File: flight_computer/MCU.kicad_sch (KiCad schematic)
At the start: 43 parts, among them J1 Conn_02x05_Odd_Even, J2 MEM2061-01-188-00-A_REVA, Q1 Q_NPN_BEC, SW1 SW_Push, SW2 SW_Push, U2 STM8S007C8T6TR, Y1 12MHz

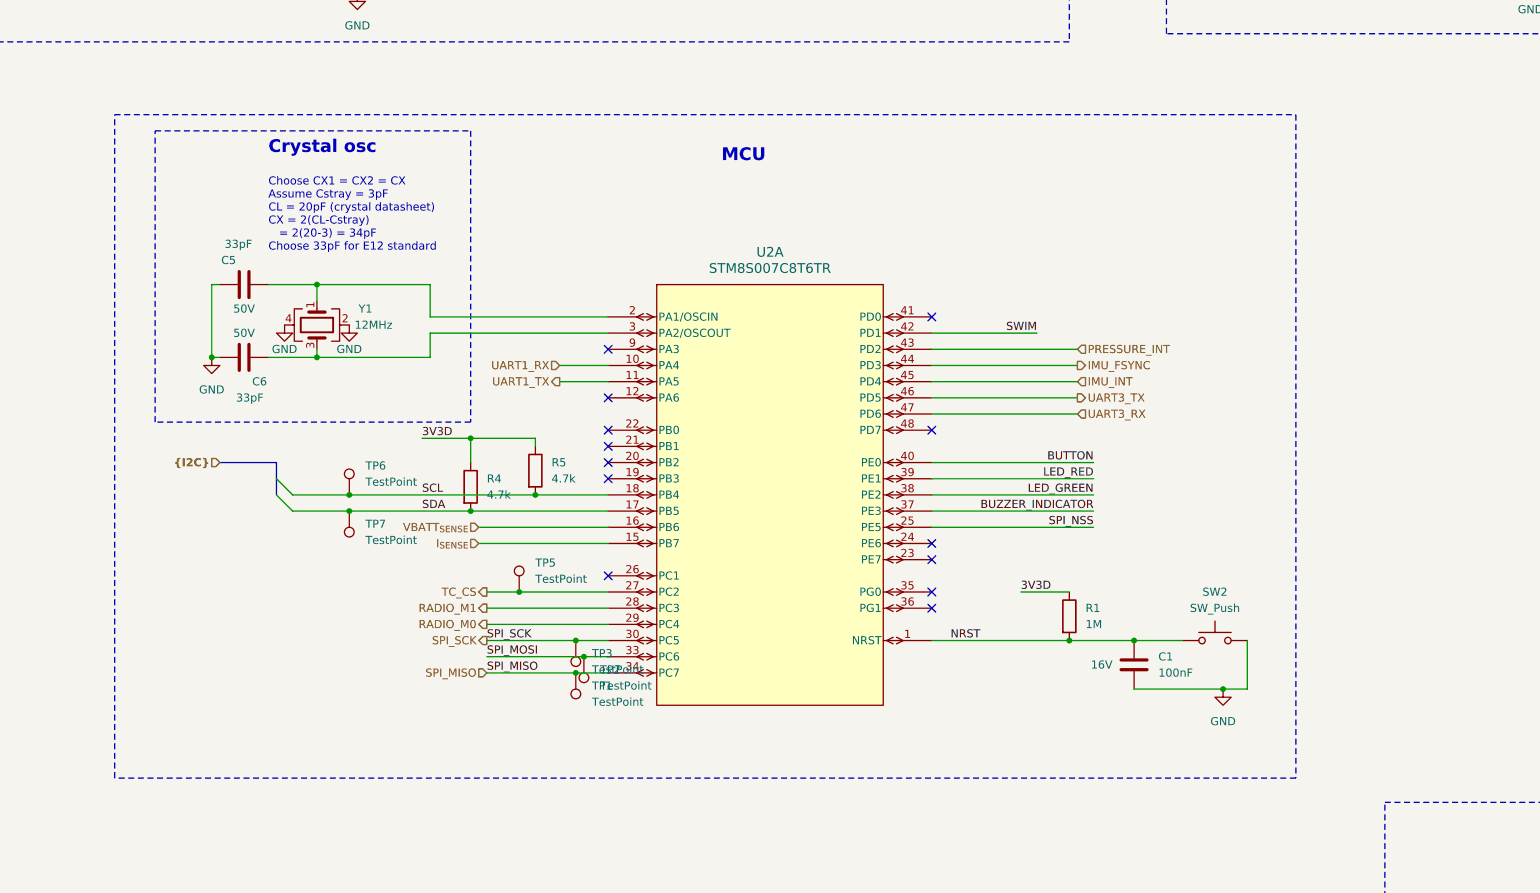
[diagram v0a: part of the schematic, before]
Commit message: First draft of PCB routing complete
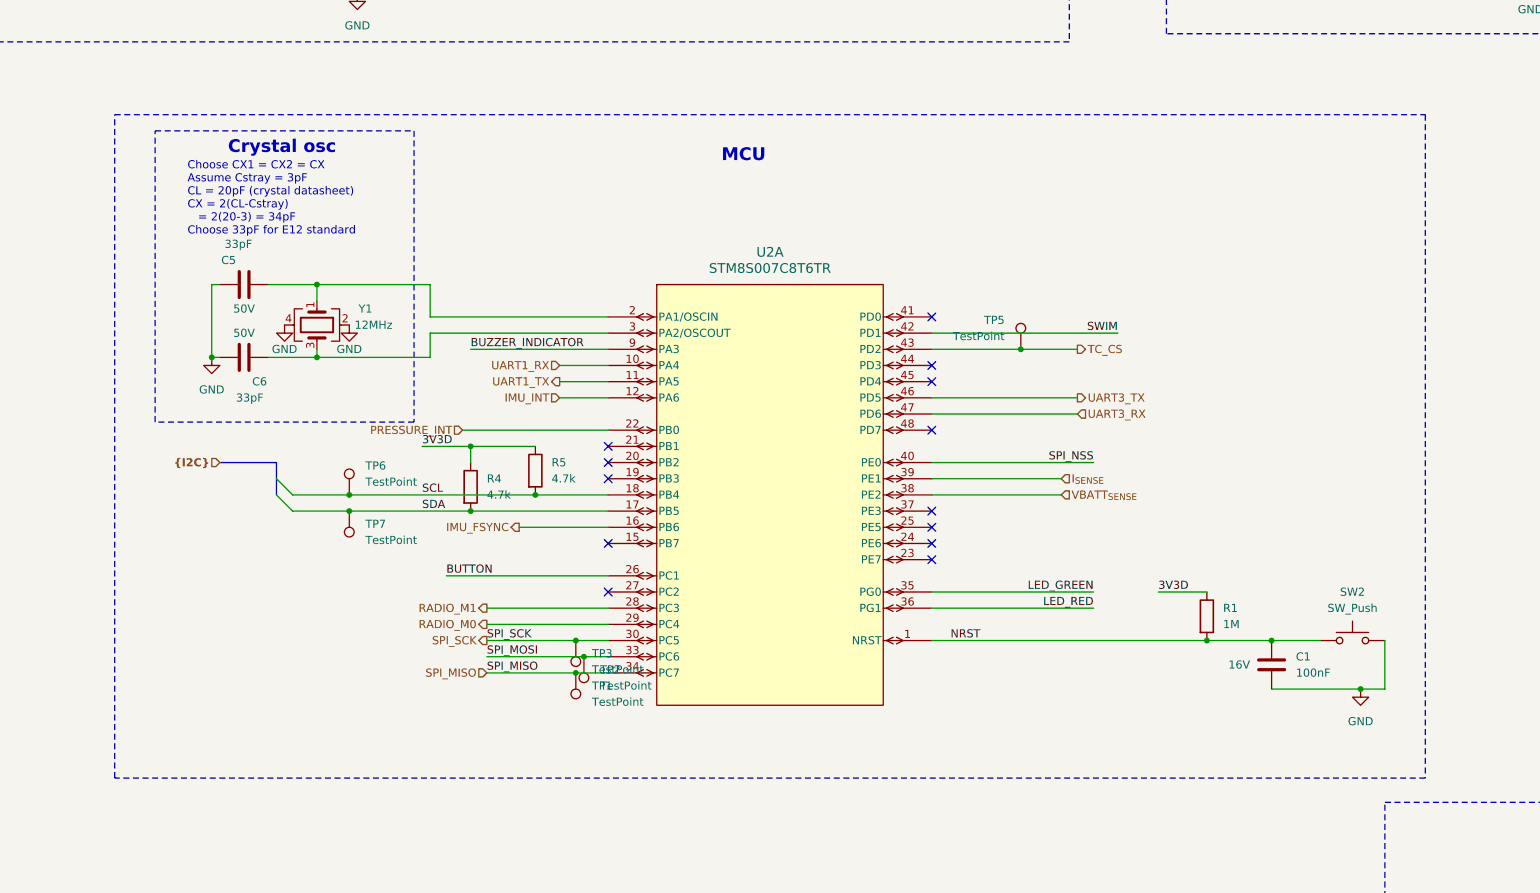
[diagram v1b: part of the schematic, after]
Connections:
- net BUTTON: now also U2.26 (PC1); no longer U2.40 (PE0)
- net BUZZER_INDICATOR: now also U2.9 (PA3); no longer U2.37 (PE3)
- net IMU_FSYNC: now also U2.16 (PB6); no longer U2.44 (PD3)
- net IMU_INT: now also U2.12 (PA6); no longer U2.45 (PD4)
- net I_{SENSE}: now also U2.39 (PE1); no longer U2.15 (PB7)
- net LED_GREEN: now also U2.35 (PG0); no longer U2.38 (PE2)
- net LED_RED: now also U2.36 (PG1); no longer U2.39 (PE1)
- net PRESSURE_INT: now also U2.22 (PB0); no longer U2.43 (PD2)
- net SPI_NSS: now also U2.40 (PE0); no longer U2.25 (PE5)
- net TC_CS: now also U2.43 (PD2); no longer U2.27 (PC2)
- net VBATT_{SENSE}: now also U2.38 (PE2); no longer U2.16 (PB6)
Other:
- moved on the sheet: C1, R1, SW2, TP5

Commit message: start of esp32
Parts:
- added C1 (x5): 100nF, Capacitor_SMD:C_0402_1005Metric, symbol Device:C
- added C1 (x2): DNP, Capacitor_SMD:C_0402_1005Metric, symbol Device:C
- added C12: 10uF, Capacitor_SMD:C_0402_1005Metric, symbol Device:C
- added C18: 10nF, Capacitor_SMD:C_0402_1005Metric, symbol Device:C
- added C40, C53: ~, Capacitor_SMD:C_0402_1005Metric, symbol Device:C
- added C46, C48, C50: 1uF, Capacitor_SMD:C_0402_1005Metric, symbol Device:C
- added L3: 0.1nH, symbol Device:L
- added L4: 24nH, symbol Device:L
- added R1: 1M, Resistor_SMD:R_0402_1005Metric, symbol Device:R
- added R31, R32, R35, R36, R37, R38, R39, R40, R41: 0R, Resistor_SMD:R_0402_1005Metric, symbol Device:R
- added R34: DNP, Resistor_SMD:R_0402_1005Metric, symbol Device:R
- added U10: ESP32-S3, Package_DFN_QFN:QFN-56-1EP_7x7mm_P0.4mm_EP5.6x5.6mm, symbol Espressif:ESP32-S3
- added Y2: 40MHz, Crystal:Crystal_SMD_3225-4Pin_3.2x2.5mm, symbol Device:Crystal_GND24
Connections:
- net 3V3A: now also C18.1, C50.1, U10.55 (VDDA), U10.56 (VDDA)
- net 3V3D: now also C1.1, C1.1, C1.1, C1.1, C12.1, C46.1, C48.1, L3.1, R1.1, R34.2, U10.20 (VDD3P3_RTC), U10.29 (VDD_SPI), U10.46 (VDD3P3_CPU)
- net GND: now also C1.1, C1.2, C1.2, C1.2, C1.2, C1.2, C1.2, C12.2, C18.2, C40.1, C46.2, C48.2, C50.2, C53.1, U10.57 (GND), Y2.2, Y2.4
- net NRST: no longer C1.1, R1.2, SW2.1, U2.1 (NRST)
- new net: C1.1, R1.2, SW2.1, U10.4 (CHIP_PU/RESET)
- new net: R37.1, U10.30 (SPIHD/GPIO27)
- new net: C53.2, L4.1, Y2.3
- new net: L4.2, U10.54 (XTAL_P)
- new net: C1.2, R1.2, R31.2
- new net: R31.1, U10.26 (GPIO20/USB_D+/ADC2_CH9)
- new net: R32.1, U10.25 (GPIO19/USB_D-/ADC2_CH8)
- new net: C1.1, R32.2
- new net: R38.1, U10.31 (SPIWP/GPIO28)
- new net: R34.1, U10.51 (GPIO45)
- new net: C40.2, U10.53 (XTAL_N), Y2.1
- new net: R39.1, U10.33 (SPICLK/GPIO30)
- new net: R40.1, U10.34 (SPIQ/GPIO31)
- new net: R41.1, U10.35 (SPID/GPIO32)
- new net: R35.2, U10.49 (U0TXD/PROG/GPIO43)
- new net: R36.2, U10.50 (U0RXD/PROG/GPIO44)
- new net VDD3P3: C1.1, L3.2, U10.2 (VDD3P3), U10.3 (VDD3P3)
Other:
- note added: "https://docs.espressif.com/projects/esp-hardware-design-guidelines/en/latest/esp32s3/esp-hardware-design-guidelines-en-master-esp32s3.pdf"
- note added: "https://www.espressif.com/sites/default/files/documentation/esp32-s3_datasheet_en.pdf"
- note added: "https://www.espressif.com/sites/default/files/documentation/esp32-s3_technical_reference_manual_en.pdf"
- moved on the sheet: C1, R1, SW2

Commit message: RevB PCB work
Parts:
- removed C1: 100nF, Capacitor_SMD:C_0402_1005Metric, symbol Device:C
- removed C48: 1uF, Capacitor_SMD:C_0402_1005Metric, symbol Device:C
- removed R37, R38, R39, R40, R41: 0R, Resistor_SMD:R_0402_1005Metric, symbol Device:R
- added J6: USB_C_Receptacle_USB2.0, symbol Connector:USB_C_Receptacle_USB2.0
- added R42: 5.1k, Resistor_SMD:R_0402_1005Metric, symbol Device:R
- added U11: USBLC6-2SC6, Package_TO_SOT_SMD:SOT-23-6, symbol Power_Protection:USBLC6-2SC6
- added U12: ESP32-S3-WROOM-1, PCM_Espressif:ESP32-S3-WROOM-1, symbol Espressif:ESP32-S3-WROOM-1
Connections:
- net 3V3D: no longer U10.29 (VDD_SPI)
- net GND: now also J6.A1 (GND), J6.A12 (GND), J6.B1 (GND), J6.B12 (GND), J6.S1 (SHIELD), R42.2, U11.2 (GND)
- net SPI_MISO: no longer TP1.1, U2.34 (PC7)
- net SPI_MOSI: no longer TP2.1, U2.33 (PC6)
- net SPI_SCK: no longer TP3.1, U2.30 (PC5)
- net at C1.2, R1.2, R31.2: now also U11.1 (I/O1)
- net at C1.1, R32.2: now also U11.3 (I/O2)
- new net: TP3.1, U2.30 (PC5)
- new net: TP2.1, U2.33 (PC6)
- new net: TP1.1, U2.34 (PC7)
- new net: U12.1 (GND), U12.40 (GND), U12.41 (GND)
- new net: J6.A5 (CC1), R42.1
- new net: J6.A7 (D-), J6.B7 (D-), U11.4 (I/O2)
- new net: J6.A6 (D+), J6.B6 (D+), U11.6 (I/O1)
- new net VBUS_5V_IN: J6.A4 (VBUS), J6.A9 (VBUS), J6.B4 (VBUS), J6.B9 (VBUS), U11.5 (VBUS)
- no-connect marks 19 -> 22
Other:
- note added: "500ma+"
- note added: "Place close to chip"
- note added: "Place close to disturbance source (connector)"
- moved on the sheet: C1, R1, R31, R32
